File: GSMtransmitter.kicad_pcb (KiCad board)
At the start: 2 copper layers, 69 x 83 mm, 120 parts, among them J1 Conn_01x06_Pin, J10 HJ-SMA405, J2 Conn_02x02_2.54, J3 Conn_01x05, J4 8P8C_DS1134, J5 Conn_DEGSON_01x02_Pin, J6 Conn_DEGSON_01x02_Pin, J7 Conn_DEGSON_01x02_Pin, J8 Conn_DEGSON_01x02_Pin, J9 1042240820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

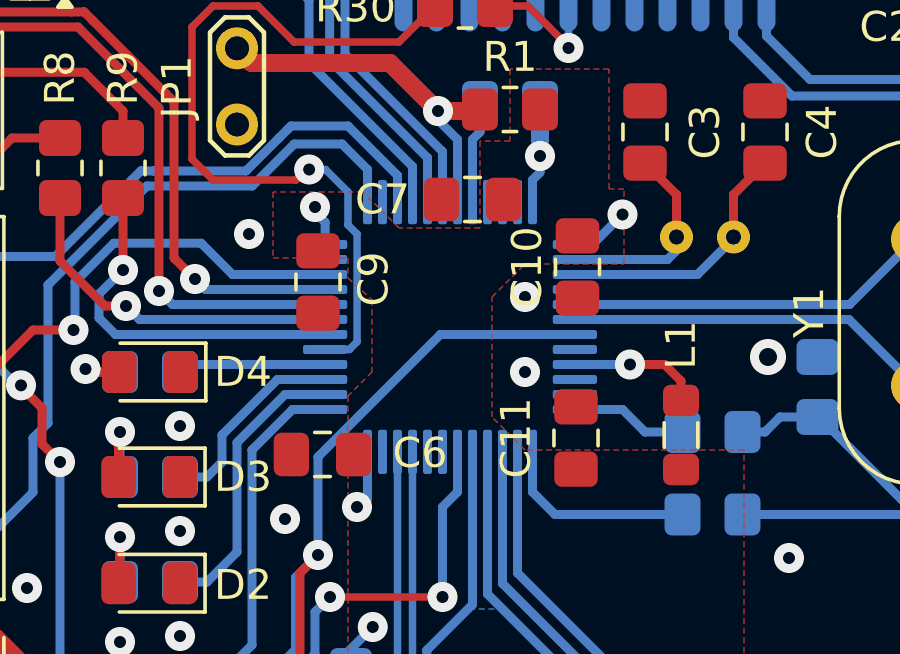
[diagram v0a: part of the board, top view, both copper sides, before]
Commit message: STM32L052 instead STM32L051
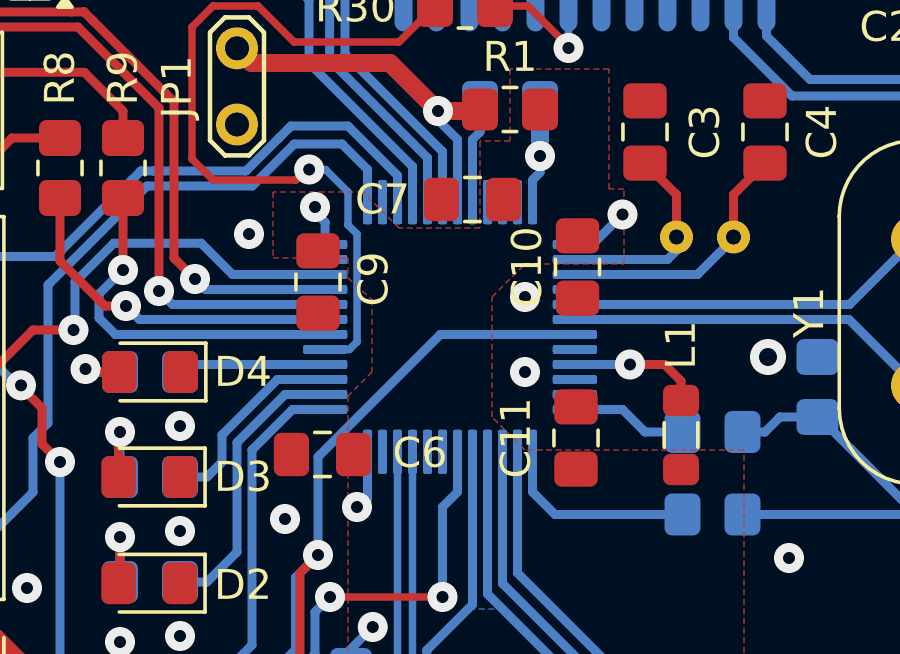
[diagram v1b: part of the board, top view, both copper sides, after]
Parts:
- added U1: STM32L052C8Tx, Package_QFP:LQFP-48_7x7mm_P0.5mm, B.Cu at (73.5, 66.0)

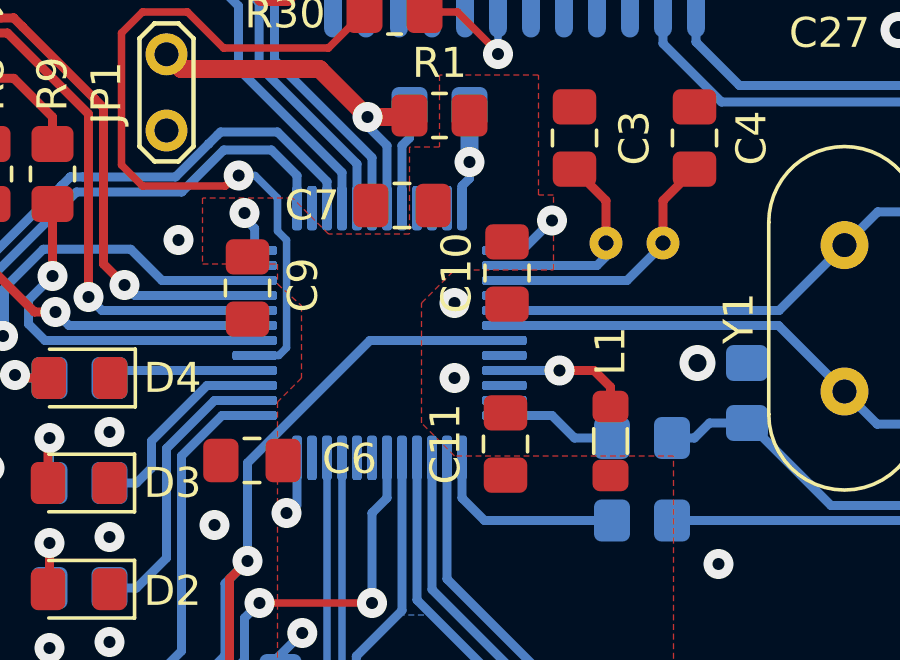
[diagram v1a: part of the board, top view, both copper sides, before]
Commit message: Wrong 32kHz clock pins fixed
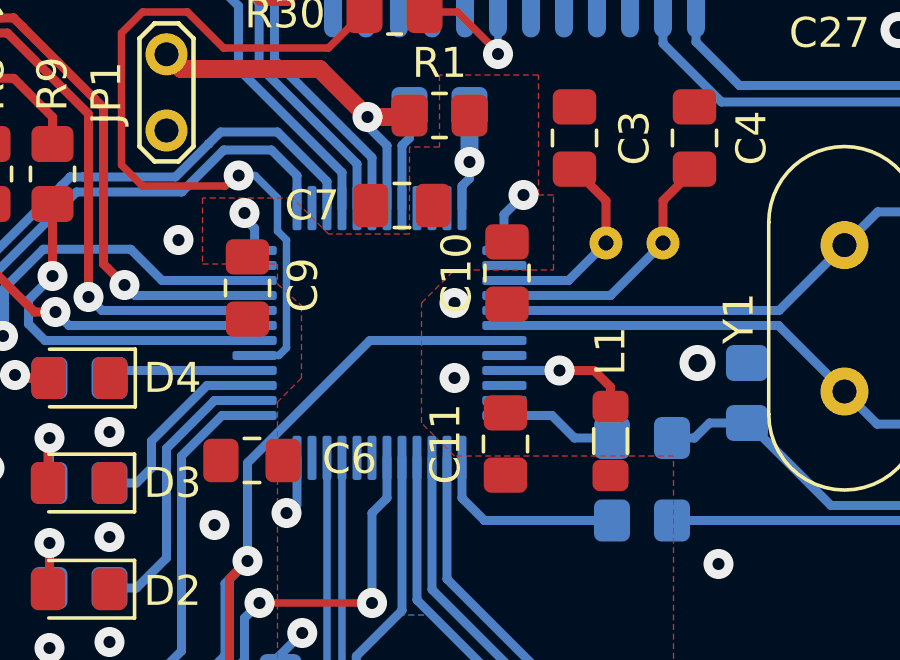
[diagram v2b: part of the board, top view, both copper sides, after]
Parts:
- removed the U1 at (73.5, 66.0)
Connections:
- C3 pad 2: Net-(U1-PC13) -> Net-(U1-PC14)
- C4 pad 2: Net-(U1-PC14) -> Net-(U1-PC15)
- U1 pad 2: Net-(U1-PC13) -> unconnected-(U1-PC13-Pad2)
- U1 pad 4: unconnected-(U1-PC15-Pad4) -> Net-(U1-PC15)
- Y2 pad 1: Net-(U1-PC14) -> Net-(U1-PC15)
- Y2 pad 2: Net-(U1-PC13) -> Net-(U1-PC14)
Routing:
- net Net-(U1-PC15): track 0.00 -> 8.91 mm
- net Net-(U1-PC13): track 6.86 -> 0.00 mm
- net Net-(U1-PC14): track 8.68 -> 6.80 mm

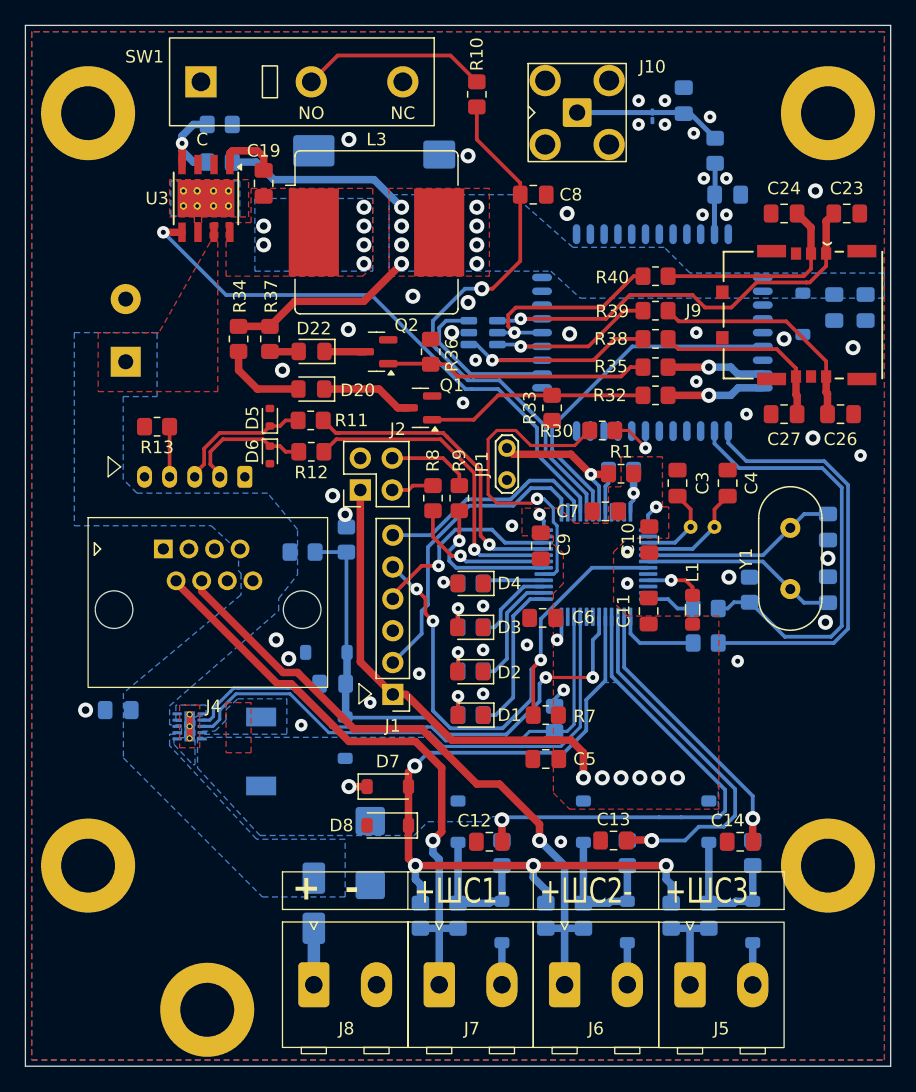
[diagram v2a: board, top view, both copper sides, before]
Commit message: 32kHz replaced
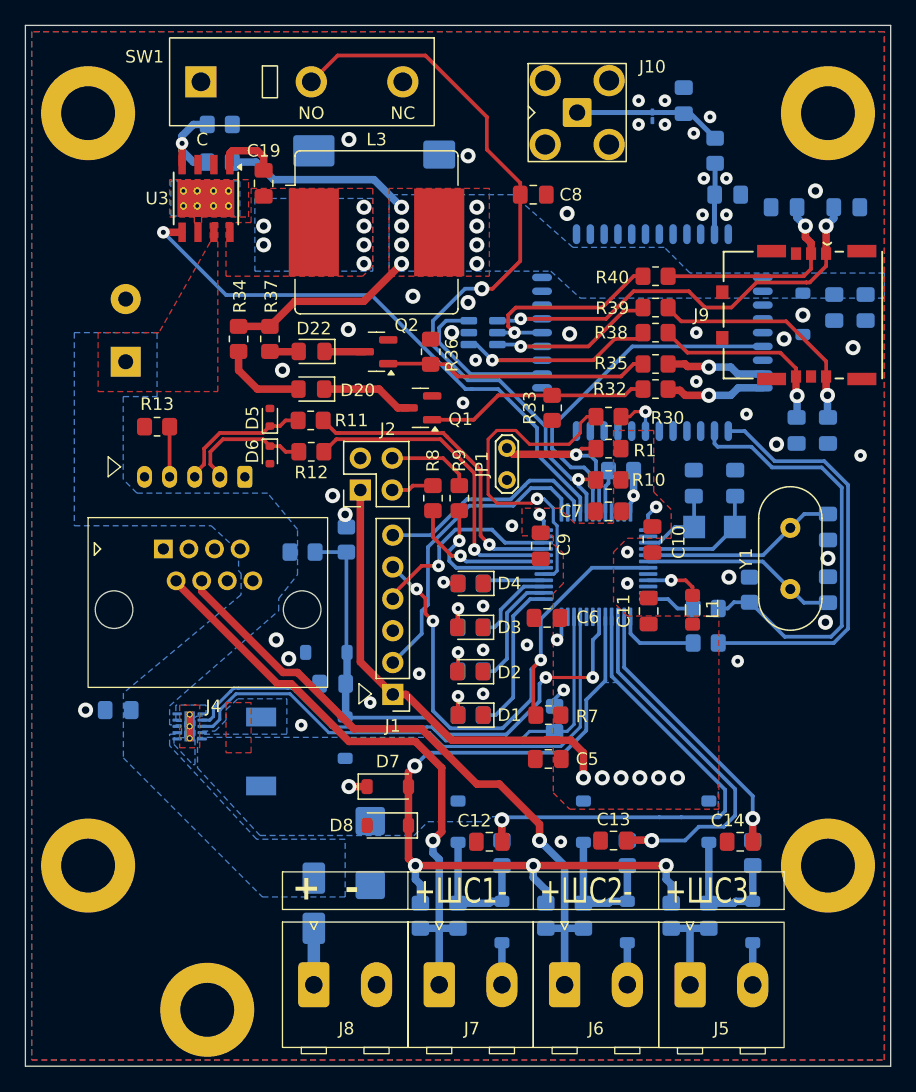
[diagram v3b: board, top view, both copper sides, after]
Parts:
- C23, C24, C26, C27, C3, C4: moved to B.Cu
- Y2: footprint Crystal:Crystal_Round_D2.0mm_Vertical -> Crystal:Crystal_SMD_EuroQuartz_EQ161-2Pin_3.2x1.5mm_HandSoldering
- moved R10 32.5 mm to (74.5, 59.2), turned to 180 degrees
- moved R1 2.24 mm to (74.5, 56.8)
- moved C26 1.64 mm to (92.0, 55.3), turned to 90 degrees
- moved C27 1.64 mm to (89.5, 55.3), turned to 90 degrees
- moved C3 1.30 mm to (81.3, 59.5)
- moved R30 1.21 mm to (74.5, 54.2)
- moved C4 0.60 mm to (84.6, 59.5)
- moved C23 0.50 mm to (93.5, 37.5)
- moved C24 0.50 mm to (88.5, 37.5)
- moved R32 0.50 mm to (78.2, 52.0)
- moved R38 0.50 mm to (78.2, 47.5)
- moved C6 0.35 mm to (69.6, 70.2)
- moved C10 0.25 mm to (78.0, 64.0)
- moved C7 0.25 mm to (74.5, 61.8)
- moved R35 0.25 mm to (78.2, 50.0)
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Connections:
- R10 pad 1: Net-(SW1-B) -> +3V3
- SW1 pad 2: Net-(SW1-B) -> /TAMPER
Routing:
- net /TAMPER: track 44.5 -> 62.0 mm, vias 1 -> 2
- net Net-(SW1-B): track 14.9 -> 0.00 mm
- net /UART2_RI: track 26.0 -> 27.3 mm
- net Net-(U1-PC15): track 8.91 -> 10.1 mm
- net Net-(JP1-B): track 12.4 -> 13.5 mm
- net Net-(D21-IO3): track 34.7 -> 35.5 mm, vias 1 -> 2
- net Net-(U4-UART1_RI): track 4.41 -> 3.67 mm
- net /RF_ENABLE: track 27.6 -> 28.2 mm
- net Net-(U4-UART1_TXD): track 34.2 -> 33.6 mm
- net /RFmodule/CARD_RST: track 16.6 -> 17.1 mm, vias 0 -> 1
- net /RFmodule/CARD_DATA: track 14.9 -> 15.1 mm, vias 0 -> 1
- net /RFmodule/CARD_CLK: track 18.5 -> 18.7 mm, vias 0 -> 1
- net GNDD: vias 49 -> 50

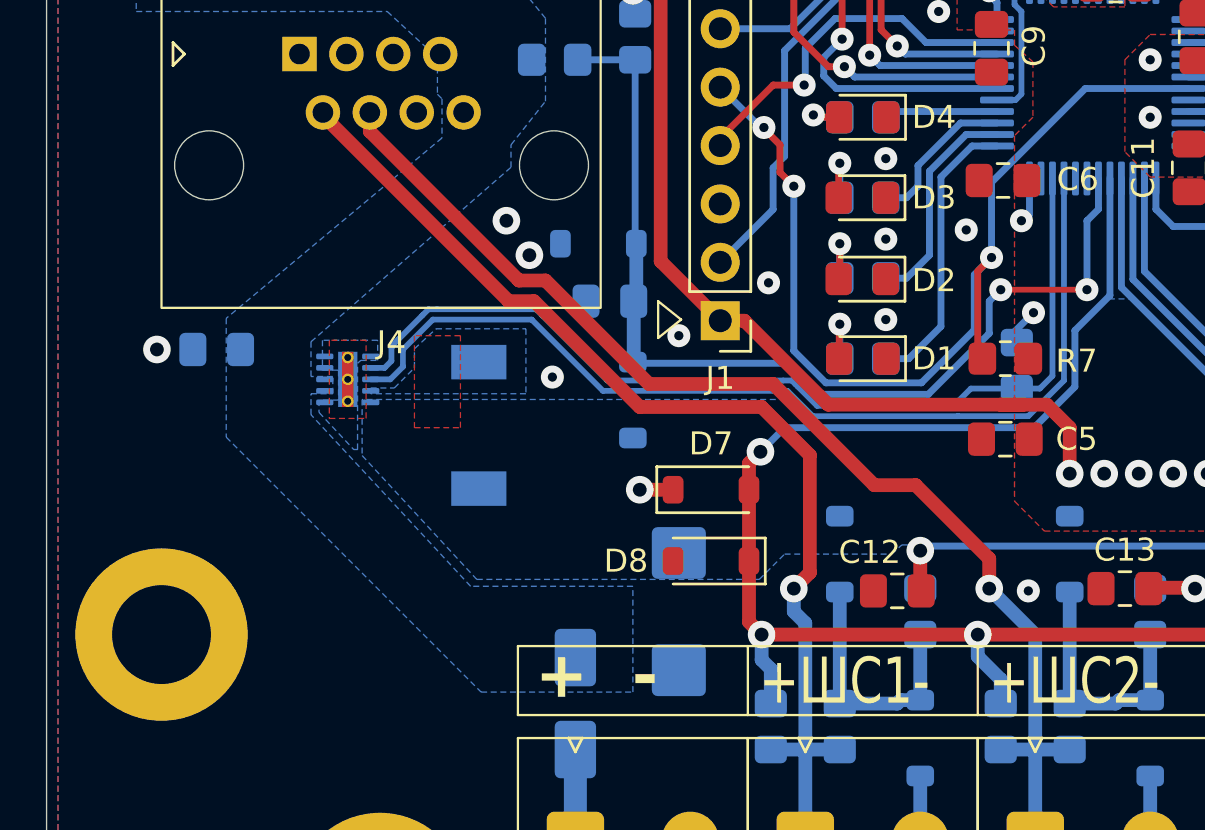
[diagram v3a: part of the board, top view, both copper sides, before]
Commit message: Inductance was replaced
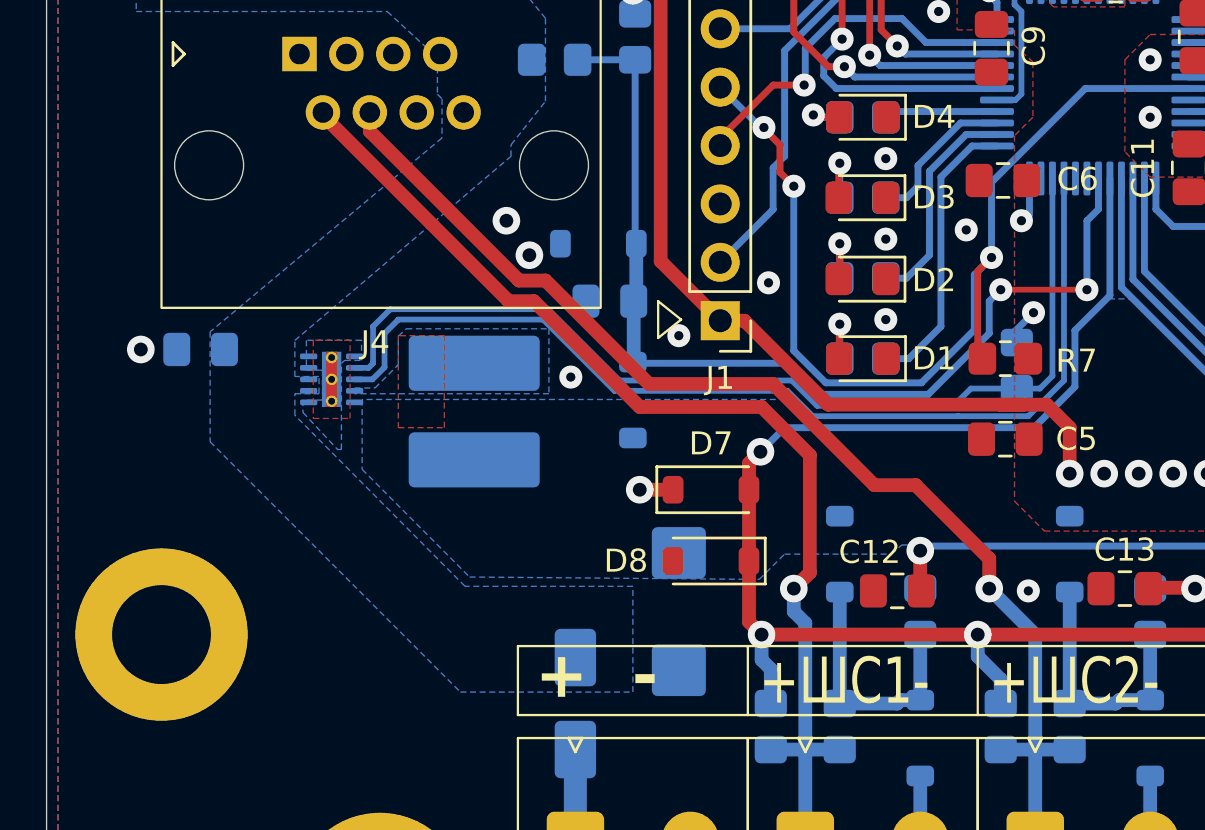
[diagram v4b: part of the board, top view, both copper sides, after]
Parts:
- C1, C2: value 18pF -> 20pF
- C18: value TAJC686M010RNJ -> CA45-C010K107T
- D1: value LED -> GNL-0805UEC
- D2, D3, D4: value LED -> GNL-0805PGC-TL
- D23: value LXES1UTAA1-158 -> LXES1UTAA1-157
- L2: value 10uH -> KSE-CD5D18NP-220NC; footprint Inductor_SMD:L_6.3x6.3_H3 -> Inductor_SMD:L_Cenker_CKCS6028
- Y1: value 8 MHz -> 4 MHz
- moved U2 0.70 mm to (40.4, 78.9)
- moved C17 0.70 mm to (34.7, 77.6)
- moved L2 0.63 mm to (46.6, 80.3)
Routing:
- net /PWR_GOOD: track 41.9 -> 43.2 mm
- net /SLEEP: track 42.8 -> 44.0 mm

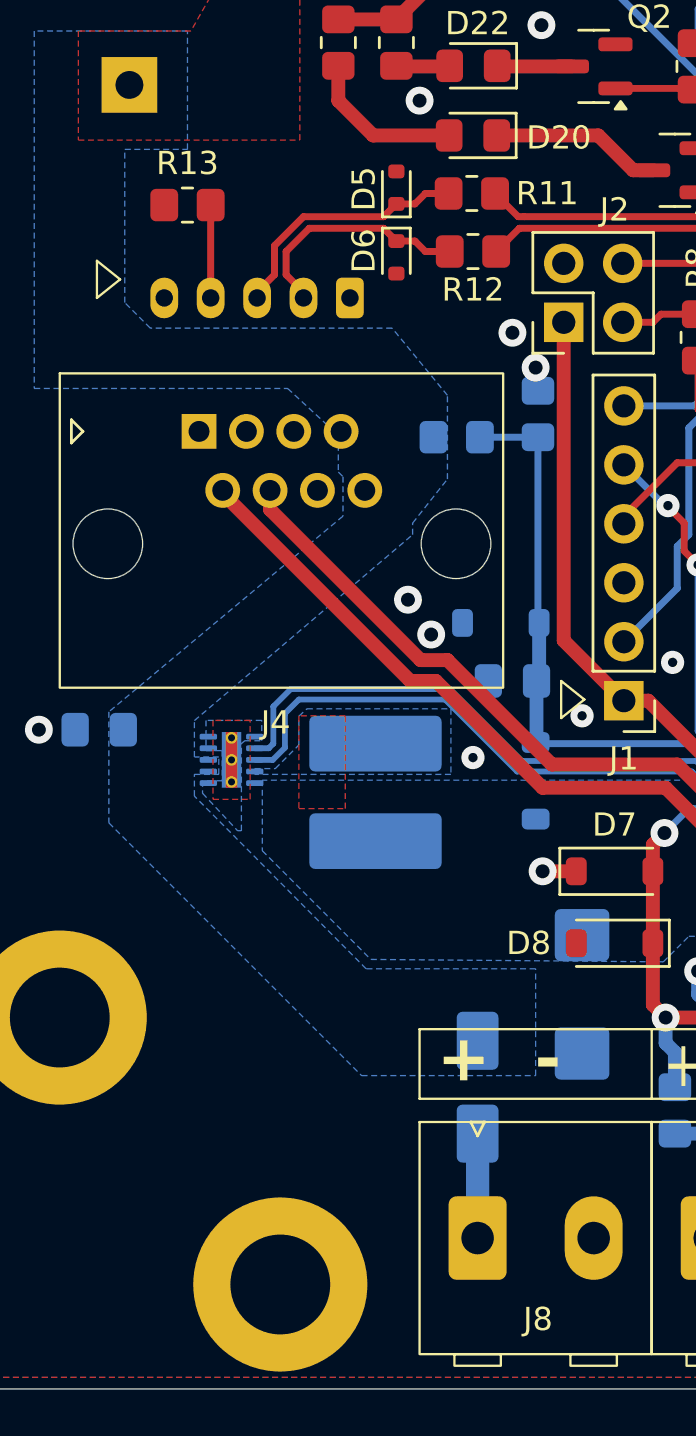
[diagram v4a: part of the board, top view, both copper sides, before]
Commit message: USB pinout fixed
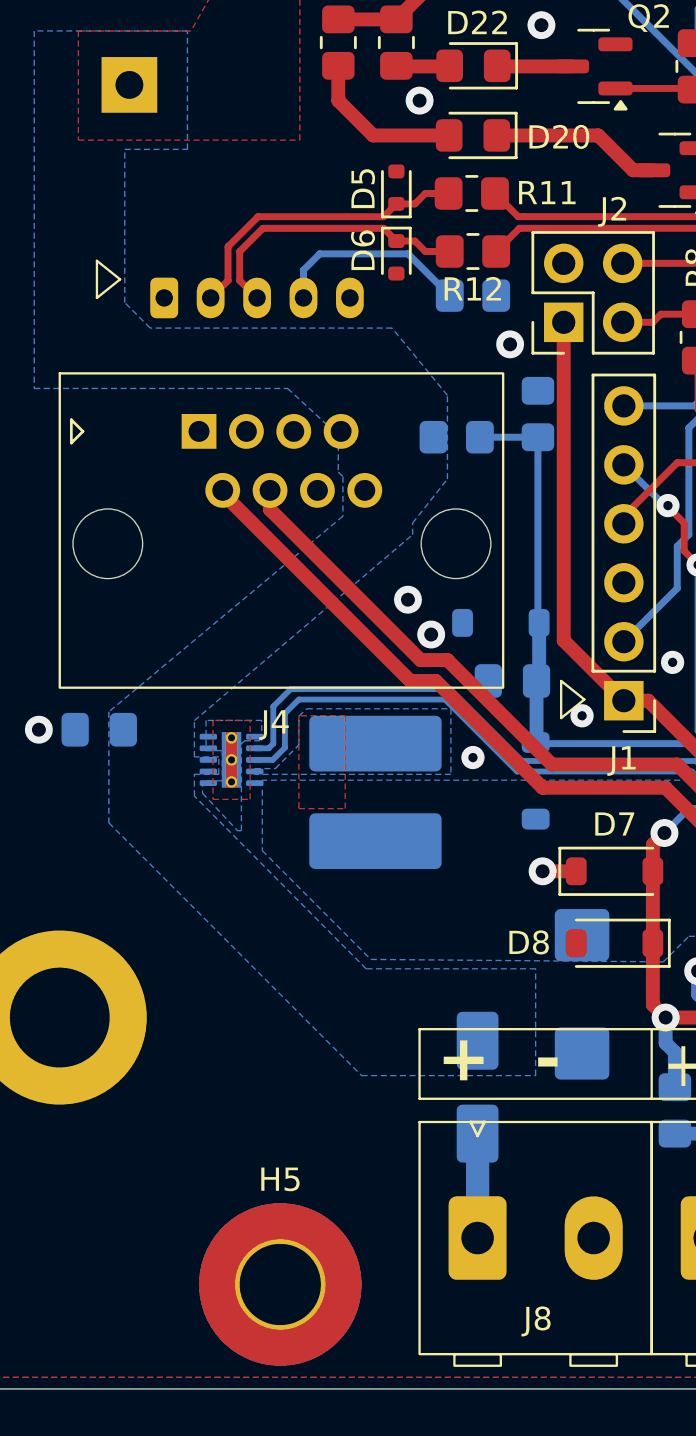
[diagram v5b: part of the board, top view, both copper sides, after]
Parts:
- H5: footprint MountingHole:MountingHole_4.3mm_M4_DIN965_Pad -> MountingHole:MountingHole_3.5mm_Pad_TopBottom
- L1: value 10uH -> MLZ2012M100WT000
- R13: moved to B.Cu
- moved R13 12.9 mm to (50.8, 58.9), turned to 0 degrees
- moved J3 8.00 mm to (37.5, 59.0), turned to 0 degrees
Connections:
- J3 pad 1: unconnected-(J3-Pin_1-Pad1) -> GNDD
- J3 pad 2: Net-(D6-K) -> Net-(D5-K)
- J3 pad 3: Net-(D5-K) -> Net-(D6-K)
- J3 pad 5: GNDD -> unconnected-(J3-Pin_5-Pad5)
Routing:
- net Net-(J3-Pin_4): track 4.00 -> 8.54 mm
- net Net-(D6-K): track 10.2 -> 12.4 mm
- net Net-(D5-K): track 11.0 -> 13.0 mm
- net GNDD: vias 50 -> 49
